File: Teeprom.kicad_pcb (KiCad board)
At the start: 2 copper layers, 16.3 x 37.3 mm, 3 parts, among them J1 Molex_DIP28_edge_contacts, U1 28C256

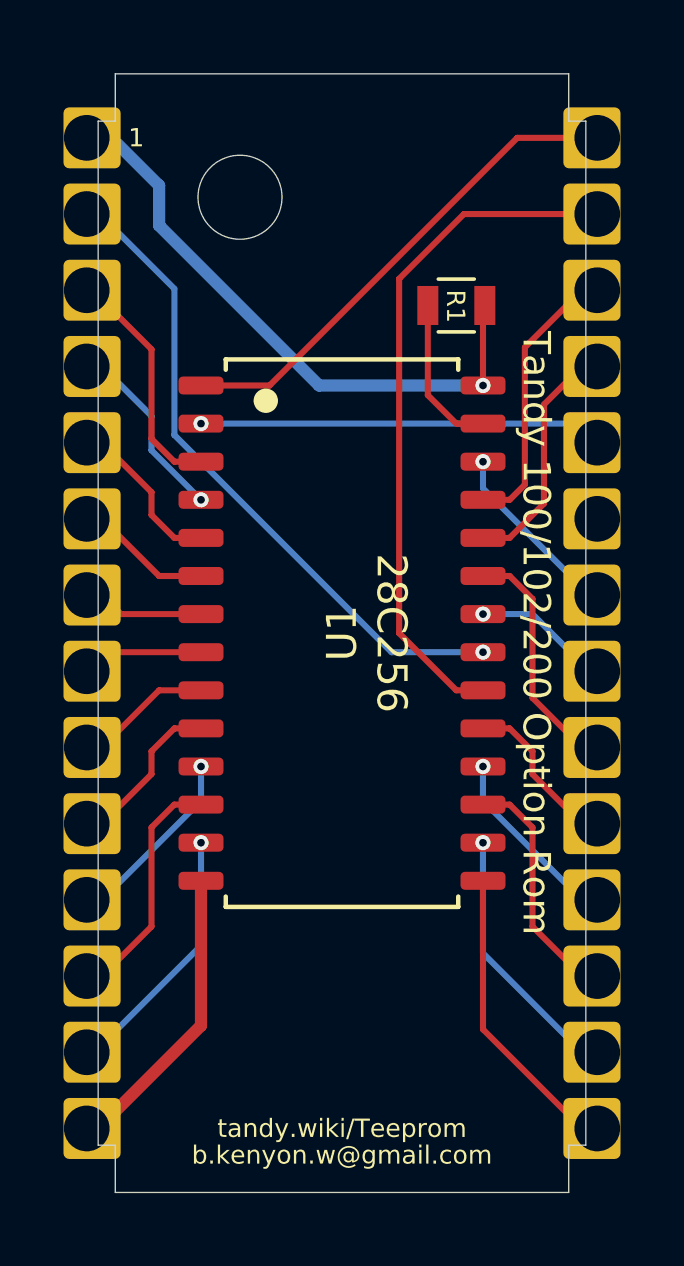
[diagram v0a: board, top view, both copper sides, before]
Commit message: update to new pcb2molex8878 template & carrier with chamfer instead of pin
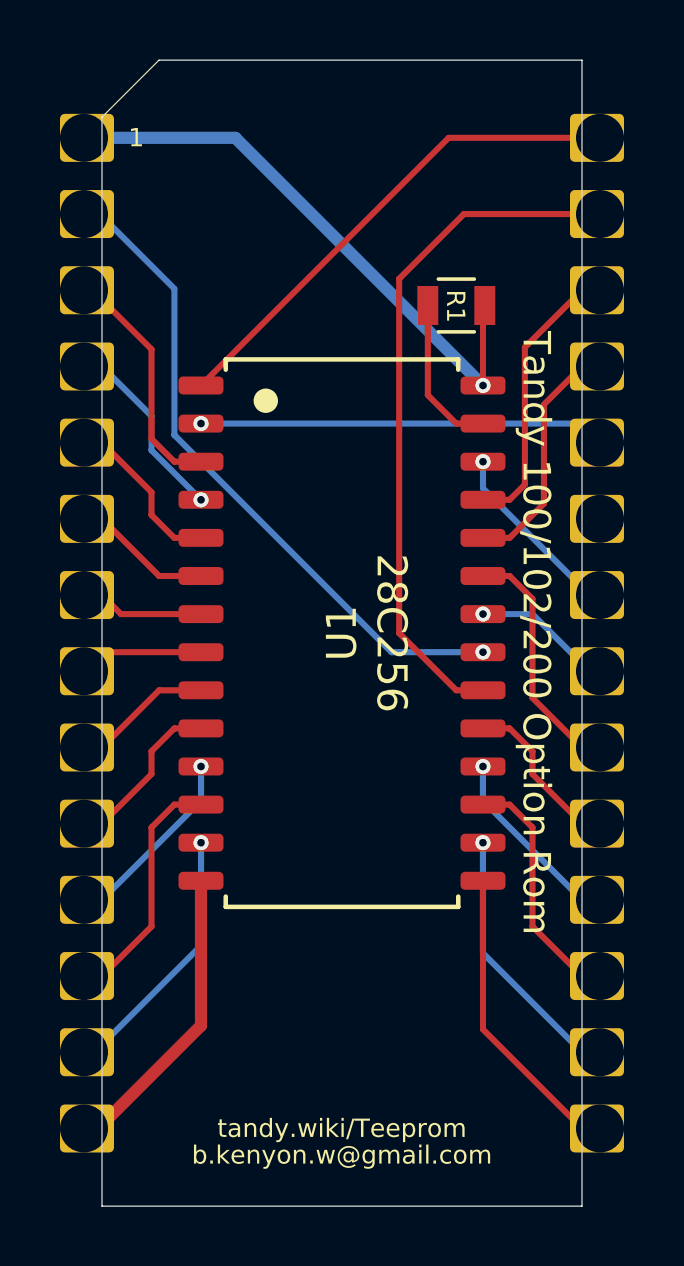
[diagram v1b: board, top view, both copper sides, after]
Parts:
- J1: footprint 000_LOCAL:Molex_50-39-5288 -> 000_LOCAL:pcb2molex8878
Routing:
- net /+5V: track 20.9 -> 18.6 mm
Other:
- board size 16.3 x 37.3 mm -> 16 x 38.2 mm
- board text added: "Use with thingiverse.com/thing:3821586"
- board text removed: "Use with thingiverse.com/thing:3723135"
